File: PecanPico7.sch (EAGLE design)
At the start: 178 parts, among them IC1 Si4060-B1B-FM, IC10 TPS62260DRVT, IC11 TPS62261DRVT, IC12 TPS63021, IC13 RF6886, IC14 TPS78227DDCR, IC16 PAC1720-1-AIA-TR, IC2 Si4060-B1B-FM, IC3 BME280_BME280, IC4 uBlox MAX7/8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

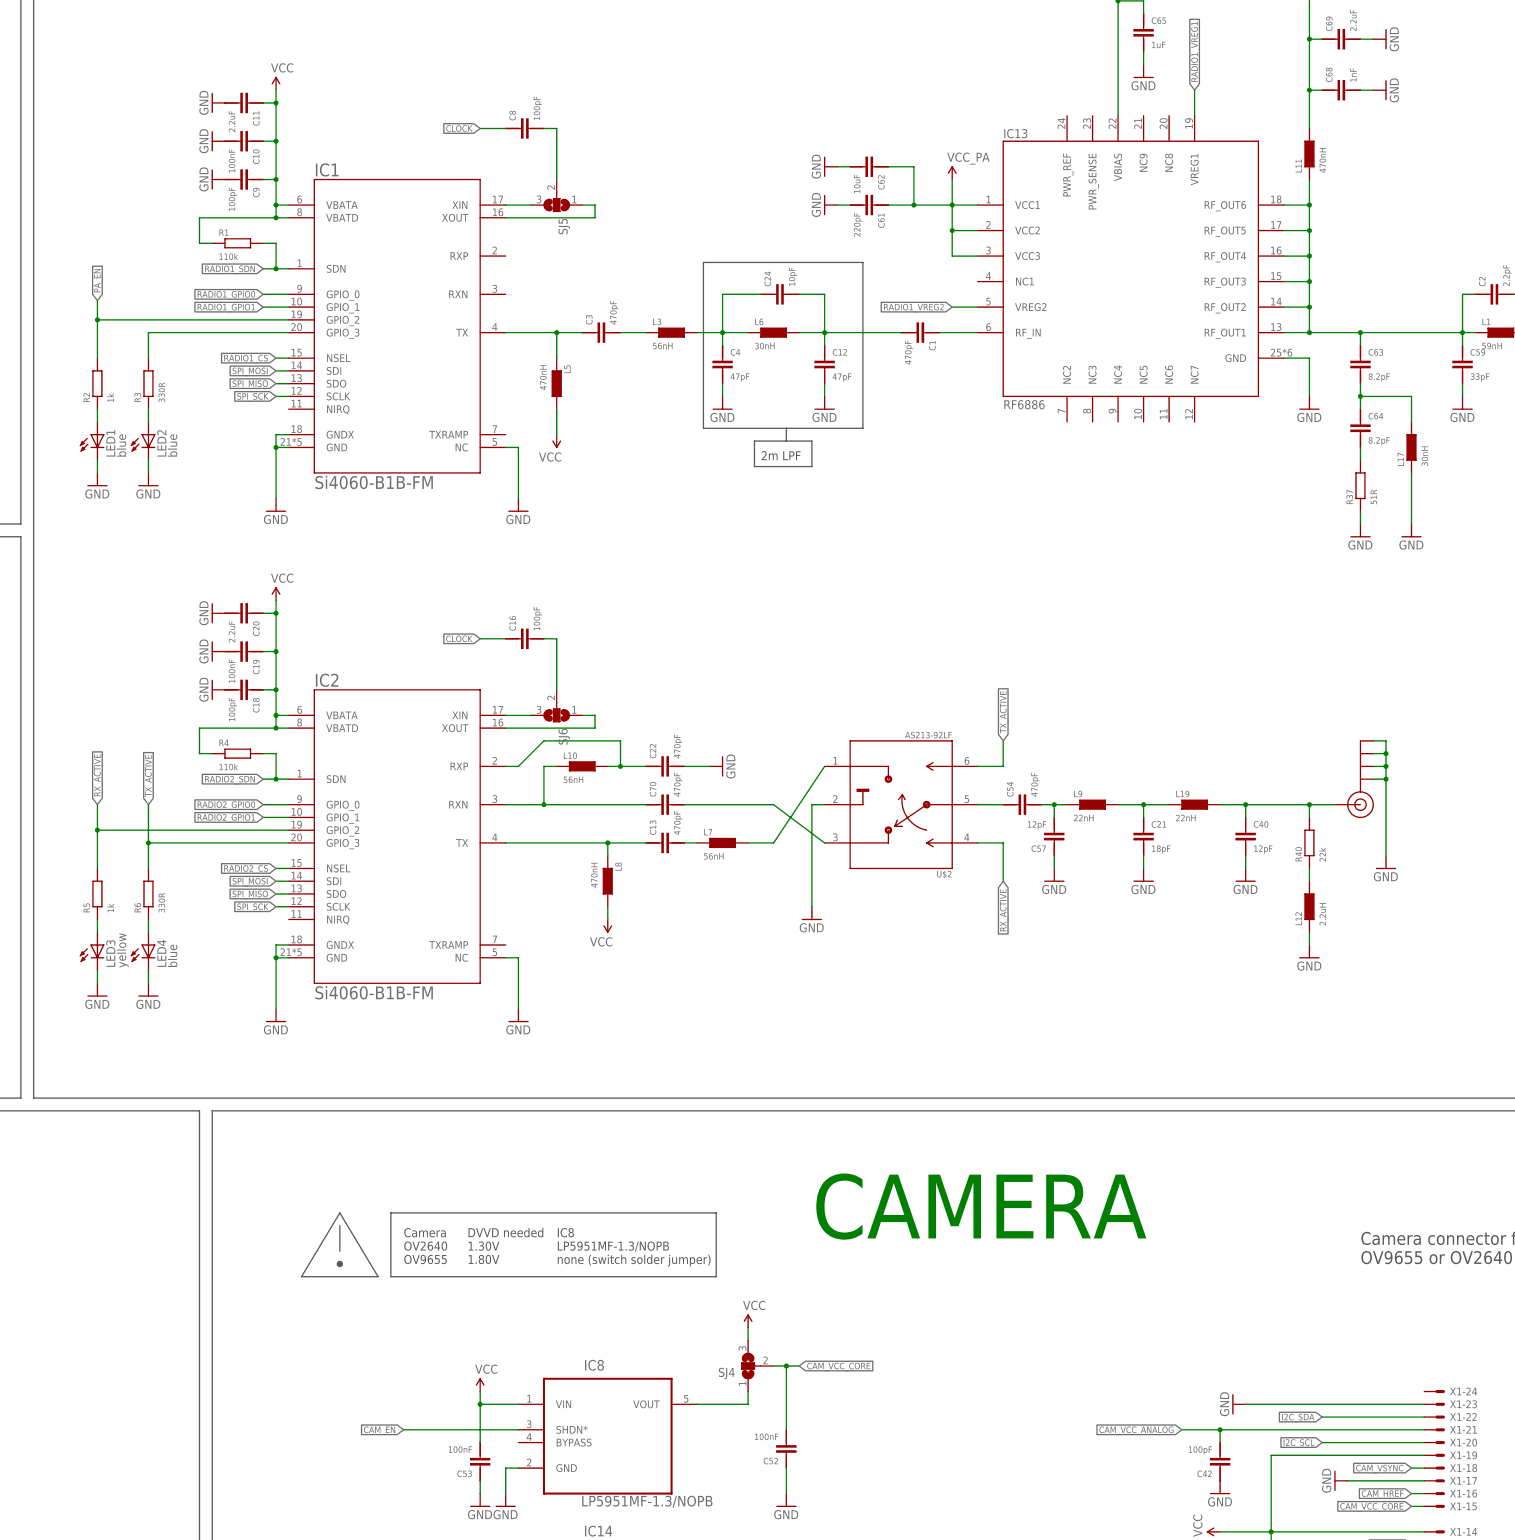
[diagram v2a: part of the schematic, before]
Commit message: Moved parts around
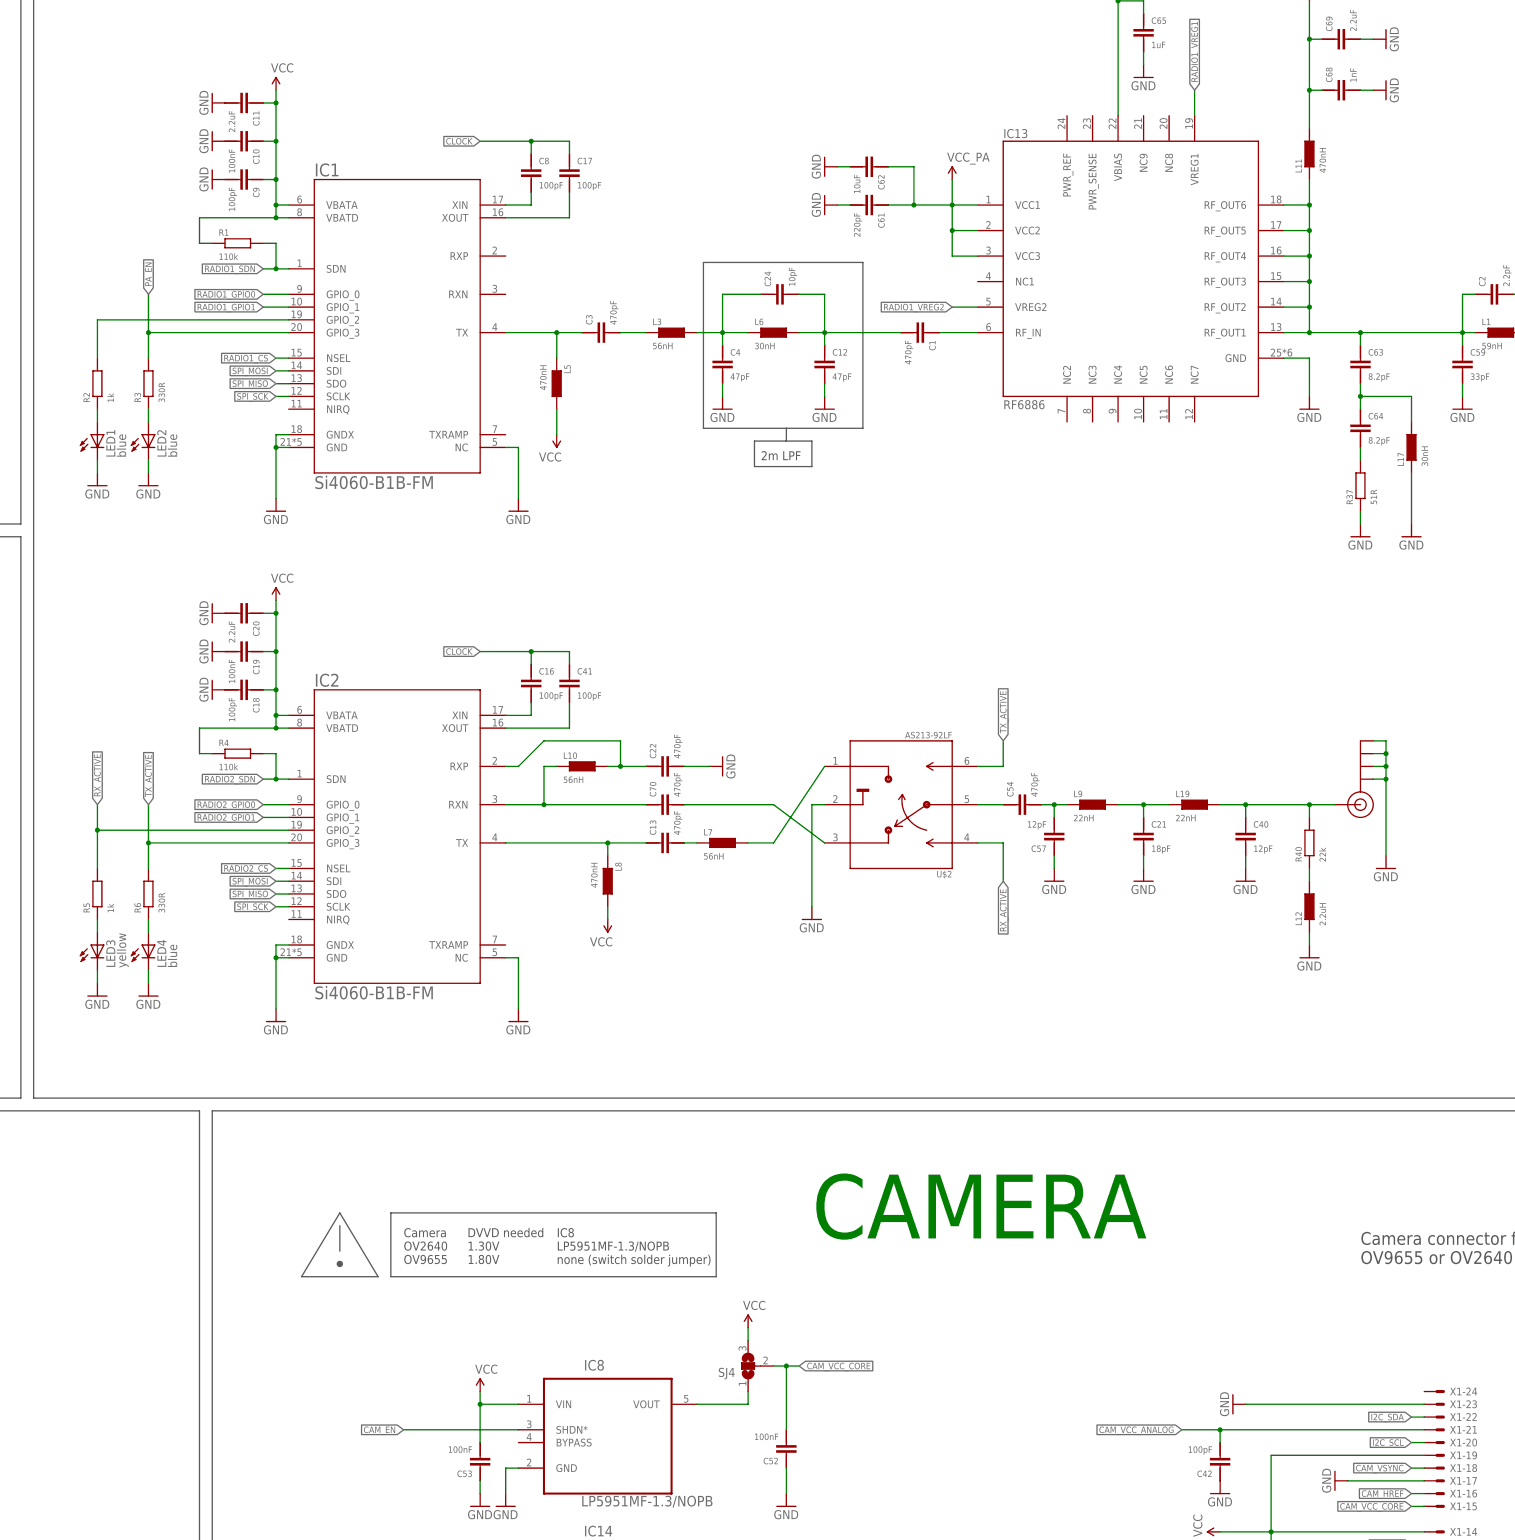
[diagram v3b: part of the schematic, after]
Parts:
- removed SJ5, SJ6: (no value), PecanPico6:SJ2W
- added C17, C41: 100pF, PecanPico6:CAP-0402
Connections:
- removed net N$34: C16.1, SJ6.2
- removed net N$8: IC1.XIN, SJ5.3
- net CLOCK: now also C17.2, C41.2
- net N$13: now also IC1.GPIO_2, R2.2; no longer IC1.GPIO_3, R3.2
- net N$18: now also C16.1; no longer SJ6.3
- net N$19: now also C41.1; no longer SJ6.1
- net N$37: now also IC1.XIN; no longer SJ5.2
- net N$9: now also C17.1; no longer SJ5.1
- net PA_EN: now also IC1.GPIO_3, R3.2; no longer IC1.GPIO_2, R2.2
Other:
- moved on the sheet: C16, C8
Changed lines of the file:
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@@
 <?xml version="1.0" encoding="utf-8"?>
 <!DOCTYPE eagle SYSTEM "eagle.dtd">
-<eagle version="7.2.0">
+<eagle version="7.3.0">
 <drawing>
 <settings>
@@
 <part name="L20" library="PecanPico6" deviceset="IND-0402" device="" value="2.2uH"/>
 <part name="C24" library="PecanPico6" deviceset="CAP-0402" device="" value="10pF"/>
-<part name="SJ5" library="PecanPico6" deviceset="SJ2W" device=""/>
-<part name="SJ6" library="PecanPico6" deviceset="SJ2W" device=""/>
 <part name="C7" library="PecanFemto3" deviceset="CAP-0805" device="" value="10uF"/>
 <part name="GND12" library="PecanPico6" deviceset="GND" device=""/>
@@
 <part name="GND123" library="PecanPico6" deviceset="GND" device=""/>
 <part name="U$3" library="PecanFemto3" deviceset="TXC_7Z" device="7Q"/>
+<part name="C17" library="PecanPico6" deviceset="CAP-0402" device="" value="100pF"/>
+<part name="C41" library="PecanPico6" deviceset="CAP-0402" device="" value="100pF"/>
 </parts>
 <sheets>
@@
 <instance part="J$1" gate="1" x="386.08" y="403.86" rot="R180"/>
 <instance part="GND5" gate="1" x="391.16" y="388.62"/>
-<instance part="C8" gate="G$1" x="144.78" y="444.5" rot="R90"/>
+<instance part="C8" gate="G$1" x="147.32" y="436.88"/>
 <instance part="GND6" gate="1" x="96.52" y="368.3"/>
 <instance part="C9" gate="G$1" x="91.44" y="434.34" rot="R270"/>
@@
 <instance part="L7" gate="G$1" x="185.42" y="302.26"/>
 <instance part="C13" gate="G$1" x="172.72" y="302.26" rot="R90"/>
-<instance part="C16" gate="G$1" x="144.78" y="342.9" rot="R90"/>
+<instance part="C16" gate="G$1" x="147.32" y="335.28"/>
 <instance part="GND13" gate="1" x="96.52" y="266.7"/>
 <instance part="C18" gate="G$1" x="91.44" y="332.74" rot="R270"/>
@@
 <instance part="L20" gate="G$1" x="373.38" y="383.54" rot="R90"/>
 <instance part="C24" gate="G$1" x="195.58" y="411.48" rot="R90"/>
-<instance part="SJ5" gate="G$1" x="152.4" y="429.26" rot="R270"/>
-<instance part="SJ6" gate="G$1" x="152.4" y="327.66" rot="R270"/>
 <instance part="C7" gate="G$1" x="-91.44" y="495.3" rot="R180"/>
 <instance part="GND12" gate="1" x="-91.44" y="505.46" rot="R180"/>
@@
 <instance part="GND123" gate="1" x="-66.04" y="469.9"/>
 <instance part="U$3" gate="TCXO" x="175.26" y="60.96"/>
+<instance part="C17" gate="G$1" x="154.94" y="436.88"/>
+<instance part="C41" gate="G$1" x="154.94" y="335.28"/>
 </instances>
 <busses>
@@
 <segment>
 <pinref part="C8" gate="G$1" pin="2"/>
-<wire x1="142.24" y1="444.5" x2="137.16" y2="444.5" width="0.1524" layer="91"/>
-<label x="137.16" y="444.5" size="1.27" layer="95" rot="R180" xref="yes"/>
+<wire x1="147.32" y1="439.42" x2="147.32" y2="441.96" width="0.1524" layer="91"/>
+<wire x1="147.32" y1="441.96" x2="137.16" y2="441.96" width="0.1524" layer="91"/>
+<label x="137.16" y="441.96" size="1.27" layer="95" rot="R180" xref="yes"/>
+<pinref part="C17" gate="G$1" pin="2"/>
+<wire x1="154.94" y1="439.42" x2="154.94" y2="441.96" width="0.1524" layer="91"/>
+<wire x1="154.94" y1="441.96" x2="147.32" y2="441.96" width="0.1524" layer="91"/>
+<junction x="147.32" y="441.96"/>
 </segment>
 <segment>
@@
 <segment>
 <pinref part="C16" gate="G$1" pin="2"/>
-<wire x1="142.24" y1="342.9" x2="137.16" y2="342.9" width="0.1524" layer="91"/>
-<label x="137.16" y="342.9" size="1.27" layer="95" rot="R180" xref="yes"/>
+<wire x1="147.32" y1="337.82" x2="147.32" y2="340.36" width="0.1524" layer="91"/>
+<wire x1="147.32" y1="340.36" x2="137.16" y2="340.36" width="0.1524" layer="91"/>
+<label x="137.16" y="340.36" size="1.27" layer="95" rot="R180" xref="yes"/>
+<pinref part="C41" gate="G$1" pin="2"/>
+<wire x1="154.94" y1="337.82" x2="154.94" y2="340.36" width="0.1524" layer="91"/>
+<wire x1="154.94" y1="340.36" x2="147.32" y2="340.36" width="0.1524" layer="91"/>
+<junction x="147.32" y="340.36"/>
 </segment>
 </net>
@@
 </segment>
 </net>
-<net name="N$8" class="0">
-<segment>
-<pinref part="IC1" gate="G$1" pin="XIN"/>
-<wire x1="142.24" y1="429.26" x2="147.32" y2="429.26" width="0.1524" layer="91"/>
-<pinref part="SJ5" gate="G$1" pin="3"/>
-</segment>
-</net>
 <net name="N$9" class="0">
 <segment>
 <pinref part="IC1" gate="G$1" pin="XOUT"/>
-<wire x1="142.24" y1="426.72" x2="160.02" y2="426.72" width="0.1524" layer="91"/>
-<wire x1="160.02" y1="426.72" x2="160.02" y2="429.26" width="0.1524" layer="91"/>
-<pinref part="SJ5" gate="G$1" pin="1"/>
-<wire x1="160.02" y1="429.26" x2="157.48" y2="429.26" width="0.1524" layer="91"/>
+<wire x1="142.24" y1="426.72" x2="154.94" y2="426.72" width="0.1524" layer="91"/>
+<pinref part="C17" gate="G$1" pin="1"/>
+<wire x1="154.94" y1="426.72" x2="154.94" y2="431.8" width="0.1524" layer="91"/>
 </segment>
 </net>
@@
 </segment>
 <segment>
-<label x="304.8" y="187.96" size="1.27" layer="95" rot="R180" xref="yes"/>
-<wire x1="325.12" y1="187.96" x2="304.8" y2="187.96" width="0.1524" layer="91"/>
+<label x="322.58" y="187.96" size="1.27" layer="95" rot="R180" xref="yes"/>
+<wire x1="325.12" y1="187.96" x2="322.58" y2="187.96" width="0.1524" layer="91"/>
 <pinref part="X1" gate="-22" pin="S"/>
 </segment>
@@
 </segment>
 <segment>
-<label x="304.8" y="182.88" size="1.27" layer="95" rot="R180" xref="yes"/>
-<wire x1="304.8" y1="182.88" x2="325.12" y2="182.88" width="0.1524" layer="91"/>
+<label x="322.58" y="182.88" size="1.27" layer="95" rot="R180" xref="yes"/>
+<wire x1="322.58" y1="182.88" x2="325.12" y2="182.88" width="0.1524" layer="91"/>
 <pinref part="X1" gate="-20" pin="S"/>
 </segment>
@@
 </segment>
 <segment>
-<pinref part="IC1" gate="G$1" pin="GPIO_2"/>
-<pinref part="R2" gate="G$1" pin="2"/>
-<wire x1="99.06" y1="406.4" x2="60.96" y2="406.4" width="0.1524" layer="91"/>
-<wire x1="60.96" y1="406.4" x2="60.96" y2="398.78" width="0.1524" layer="91"/>
-<wire x1="60.96" y1="406.4" x2="60.96" y2="410.21" width="0.1524" layer="91"/>
-<junction x="60.96" y="406.4"/>
-<label x="60.96" y="410.21" size="1.27" layer="95" rot="R90" xref="yes"/>
+<pinref part="R3" gate="G$1" pin="2"/>
+<pinref part="IC1" gate="G$1" pin="GPIO_3"/>
+<wire x1="71.12" y1="398.78" x2="71.12" y2="403.86" width="0.1524" layer="91"/>
+<wire x1="71.12" y1="403.86" x2="99.06" y2="403.86" width="0.1524" layer="91"/>
+<wire x1="71.12" y1="403.86" x2="71.12" y2="411.48" width="0.1524" layer="91"/>
+<junction x="71.12" y="403.86"/>
+<label x="71.12" y="411.48" size="1.27" layer="95" rot="R90" xref="yes"/>
 </segment>
 </net>
@@
 <pinref part="IC2" gate="G$1" pin="XIN"/>
 <wire x1="142.24" y1="327.66" x2="147.32" y2="327.66" width="0.1524" layer="91"/>
-<pinref part="SJ6" gate="G$1" pin="3"/>
+<pinref part="C16" gate="G$1" pin="1"/>
+<wire x1="147.32" y1="327.66" x2="147.32" y2="330.2" width="0.1524" layer="91"/>
 </segment>
 </net>
@@
 <segment>
 <pinref part="IC2" gate="G$1" pin="XOUT"/>
-<wire x1="142.24" y1="325.12" x2="160.02" y2="325.12" width="0.1524" layer="91"/>
-<wire x1="160.02" y1="325.12" x2="160.02" y2="327.66" width="0.1524" layer="91"/>
-<pinref part="SJ6" gate="G$1" pin="1"/>
-<wire x1="160.02" y1="327.66" x2="157.48" y2="327.66" width="0.1524" layer="91"/>
+<wire x1="142.24" y1="325.12" x2="154.94" y2="325.12" width="0.1524" layer="91"/>
+<pinref part="C41" gate="G$1" pin="1"/>
+<wire x1="154.94" y1="325.12" x2="154.94" y2="330.2" width="0.1524" layer="91"/>
 </segment>
 </net>
@@
 </segment>
 </net>
-<net name="N$34" class="0">
-<segment>
-<pinref part="C16" gate="G$1" pin="1"/>
-<wire x1="149.86" y1="342.9" x2="152.4" y2="342.9" width="0.1524" layer="91"/>
-<pinref part="SJ6" gate="G$1" pin="2"/>
-<wire x1="152.4" y1="342.9" x2="152.4" y2="332.74" width="0.1524" layer="91"/>
-</segment>
-</net>
 <net name="N$37" class="0">
 <segment>
 <pinref part="C8" gate="G$1" pin="1"/>
-<wire x1="149.86" y1="444.5" x2="152.4" y2="444.5" width="0.1524" layer="91"/>
-<pinref part="SJ5" gate="G$1" pin="2"/>
-<wire x1="152.4" y1="444.5" x2="152.4" y2="434.34" width="0.1524" layer="91"/>
+<wire x1="147.32" y1="431.8" x2="147.32" y2="429.26" width="0.1524" layer="91"/>
+<pinref part="IC1" gate="G$1" pin="XIN"/>
+<wire x1="142.24" y1="429.26" x2="147.32" y2="429.26" width="0.1524" layer="91"/>
 </segment>
 </net>
@@
 </segment>
 </net>
-<net name="N$13" class="0">
-<segment>
-<pinref part="R3" gate="G$1" pin="2"/>
-<pinref part="IC1" gate="G$1" pin="GPIO_3"/>
-<wire x1="71.12" y1="398.78" x2="71.12" y2="403.86" width="0.1524" layer="91"/>
-<wire x1="71.12" y1="403.86" x2="99.06" y2="403.86" width="0.1524" layer="91"/>
-</segment>
-</net>
 <net name="CAM_VCC_ANALOG" class="0">
 <segment>
@@
 </segment>
 </net>
+<net name="N$13" class="0">
+<segment>
+<pinref part="IC1" gate="G$1" pin="GPIO_2"/>
+<pinref part="R2" gate="G$1" pin="2"/>
+<wire x1="99.06" y1="406.4" x2="60.96" y2="406.4" width="0.1524" layer="91"/>
+<wire x1="60.96" y1="406.4" x2="60.96" y2="398.78" width="0.1524" layer="91"/>
+</segment>
+</net>

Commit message: Connected radio GPIOs to one UART TX
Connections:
- net RADIO2_GPIO1: now also IC5G$1.PD5; no longer IC5G$1.PD15
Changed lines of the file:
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@@
 </segment>
 <segment>
-<pinref part="IC5" gate="G$1" pin="PD15"/>
-<wire x1="-144.78" y1="142.24" x2="-139.7" y2="142.24" width="0.1524" layer="91"/>
-<label x="-139.7" y="142.24" size="1.27" layer="95" xref="yes"/>
+<label x="-139.7" y="167.64" size="1.27" layer="95" xref="yes"/>
+<pinref part="IC5" gate="G$1" pin="PD5"/>
+<wire x1="-139.7" y1="167.64" x2="-144.78" y2="167.64" width="0.1524" layer="91"/>
 </segment>
 </net>

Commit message: Modified voltage supply of camera
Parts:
- removed C51: 100pF, PecanPico6:CAP-0402
- removed SJ4: (no value), PecanPico6:SJ2W
- added R10: DIODE, PecanPico6:RES-0402
- added R22: 10k, PecanPico6:RES-0402
- IC8: value LP5951MF-1.3/NOPB -> TI TC1185-1.8VCT713
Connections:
- removed net N$57: IC8.VOUT, SJ4.1
- new net N$12: C43.1, R10.2, X1-15.S
- net CAM_VCC_CORE: now also IC8.VOUT, R10.1, X1-14.S, X1-19.S; no longer SJ4.2, X1-15.S
- net CLOCK: now also R22.2; no longer C51.1
- net N$39: now also R22.1; no longer C51.2
- net N$54: now also IC4.14_VCC_RF; no longer IC4.15_RESERVED
- net VBAT_OUT: now also C53.1, IC8.VIN
- net VCC: no longer C43.1, C53.1, IC8.VIN, SJ4.3, X1-14.S, X1-19.S
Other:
- moved on the sheet: C43, C52, SJ1
